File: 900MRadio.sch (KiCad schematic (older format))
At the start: 59 parts, among them P3 BNC, P4 BNC, U3 CC1120, U4 CC1190, U6 0900PC15J0013, U7 EPCOS_B3588, X2 FA-20H32.0000MF20X-K3

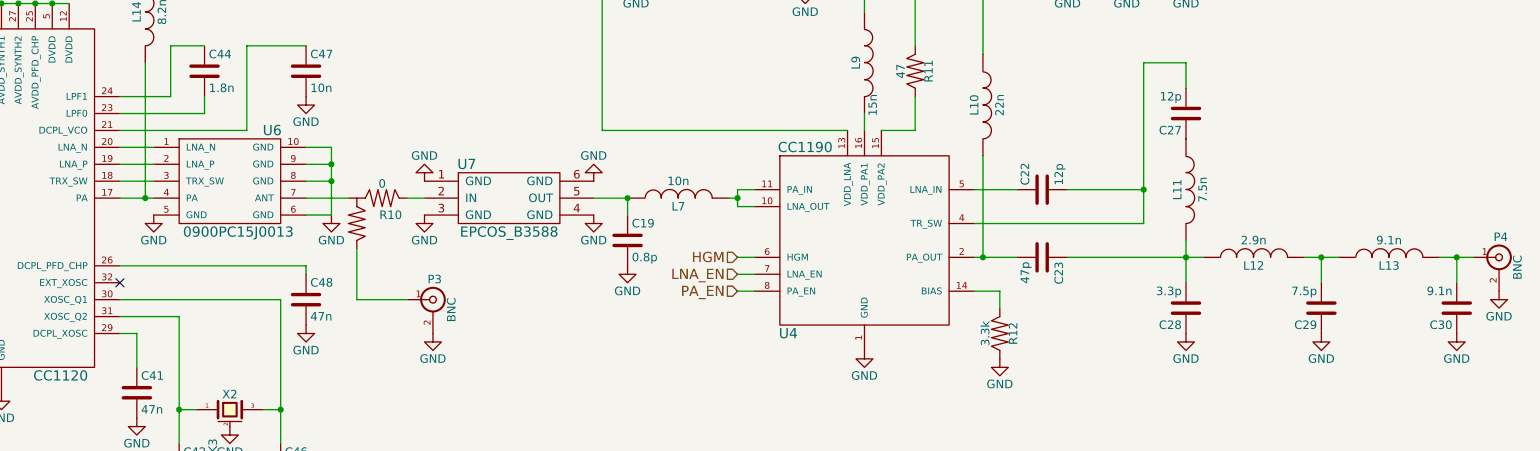
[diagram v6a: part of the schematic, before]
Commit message: Silk cleanup and some more routing finessing.
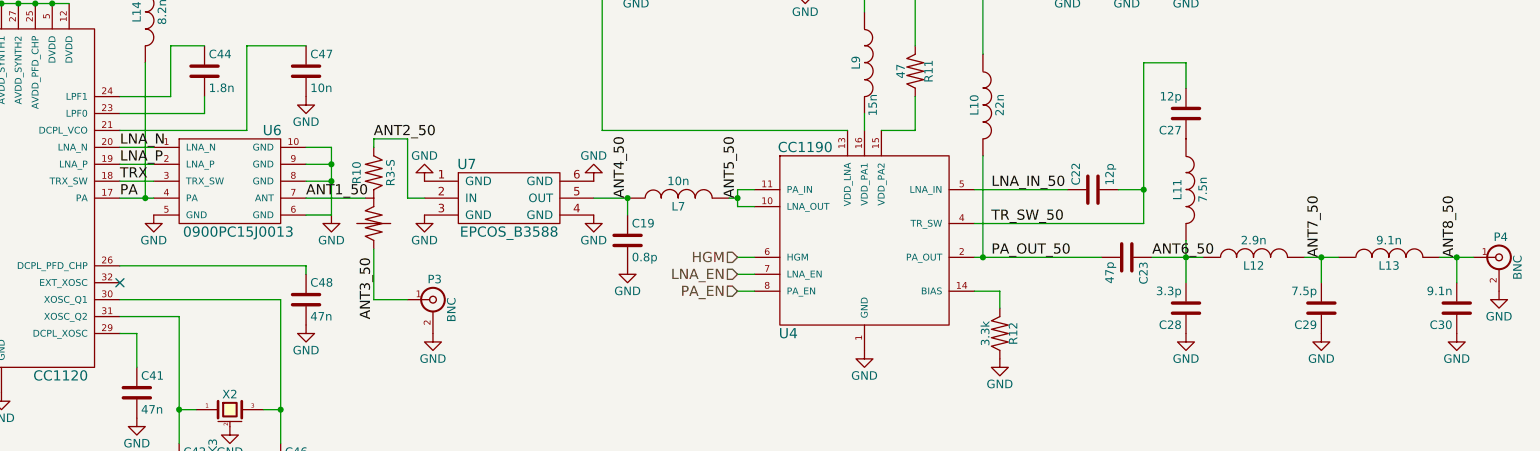
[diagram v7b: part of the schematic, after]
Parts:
- removed R10: 0, Resistors_SMD:R3_LH_0402, symbol R3-LH
- added R10: R3-S, Resistors_SMD:R3_S_0402, symbol R3-S
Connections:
- net PA: now reaches L14.2, U3.17 (PA), U6.4 (PA)
- net TRX: now reaches U3.18 (TRX_SW), U6.3 (TRX_SW)
- net LNA_P: now reaches U3.19 (LNA_P), U6.2 (LNA_P)
- net LNA_N: now reaches U3.20 (LNA_N), U6.1 (LNA_N)
- net ANT5_50: now reaches L7.2, U4.10 (LNA_OUT), U4.11 (PA_IN)
- net PA_OUT_50: now reaches C23.2, L10.2, U4.2 (PA_OUT)
- net TR_SW_50: now reaches C22.2, C27.2, U4.4 (TR_SW)
- net LNA_IN_50: now reaches C22.1, U4.5 (LNA_IN)
- net ANT1_50: now reaches U6.7 (ANT)
- net ANT1_50: now also R10.2
- net ANT8_50: now reaches C30.2, L13.2, P4.1 (In)
- net ANT3_50: now reaches P3.1 (In)
- net ANT3_50: now also R10.3
- net ANT2_50: now reaches U7.2 (IN)
- net ANT2_50: now also R10.1
- net ANT4_50: now reaches C19.1, L7.1, U7.5 (OUT)
- net ANT6_50: now reaches C23.1, C28.2, L11.2, L12.1
- net ANT7_50: now reaches C29.2, L12.2, L13.1
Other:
- moved on the sheet: C22, C23
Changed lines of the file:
@@
-$EndComp
-$Comp
-L R3-LH R10
-U 1 1 55A1928A
-P 4350 3850
-F 0 "R10" H 4300 3950 50  0000 C CNN
-F 1 "0" H 4350 3765 50  0000 C CNN
-F 2 "Resistors_SMD:R3_LH_0402" H 4350 3780 30  0001 C CNN
-F 3 "" V 4350 3850 30  0000 C CNN
-	1    4350 3850
-	-1   0    0    1
 $EndComp
 $Comp
 L C C23
 U 1 1 55A19D87
-P 8250 4200
-F 0 "C23" H 8275 4300 50  0000 L CNN
-F 1 "47p" H 8275 4100 50  0000 L CNN
-F 2 "Capacitors_SMD:C_0402" H 8288 4050 30  0001 C CNN
-F 3 "" H 8250 4200 60  0000 C CNN
-	1    8250 4200
+P 8750 4200
+F 0 "C23" H 8775 4300 50  0000 L CNN
+F 1 "47p" H 8775 4100 50  0000 L CNN
+F 2 "Capacitors_SMD:C_0402" H 8788 4050 30  0001 C CNN
+F 3 "" H 8750 4200 60  0000 C CNN
+	1    8750 4200
 	0    1    1    0
 $EndComp
@@
 L C C22
 U 1 1 55A1A99C
-P 8250 3800
-F 0 "C22" H 8275 3900 50  0000 L CNN
-F 1 "12p" H 8275 3700 50  0000 L CNN
-F 2 "Capacitors_SMD:C_0402" H 8288 3650 30  0001 C CNN
-F 3 "" H 8250 3800 60  0000 C CNN
-	1    8250 3800
+P 8550 3800
+F 0 "C22" H 8575 3900 50  0000 L CNN
+F 1 "12p" H 8575 3700 50  0000 L CNN
+F 2 "Capacitors_SMD:C_0402" H 8588 3650 30  0001 C CNN
+F 3 "" H 8550 3800 60  0000 C CNN
+	1    8550 3800
 	0    -1   -1   0
 $EndComp
@@
 	8000 4400 7850 4400
 Wire Wire Line
-	3900 3850 4150 3850
+	3900 3850 4250 3850
 Wire Wire Line
 	4500 3850 4600 3850
 Wire Wire Line
-	4200 4150 4200 4450
-Wire Wire Line
-	4200 4450 4500 4450
-Wire Wire Line
-	7850 4200 8100 4200
+	4300 4150 4300 4450
+Wire Wire Line
+	4300 4450 4500 4450
+Wire Wire Line
+	7850 4200 8600 4200
 Wire Wire Line
 	7900 4200 7900 3600
 Connection ~ 7900 4200
 Wire Wire Line
-	8400 4200 9200 4200
+	8900 4200 9200 4200
 Wire Wire Line
 	9800 4200 10000 4200
@@
 	9100 3050 9100 3200
 Wire Wire Line
-	7850 3800 8100 3800
-Wire Wire Line
-	8400 3800 8850 3800
+	7850 3800 8400 3800
+Wire Wire Line
+	8700 3800 8850 3800
 Connection ~ 8850 3800
 Wire Wire Line
@@
 Text Label 2650 650  0    60   ~ 0
 VDD_CC1120_ISO
+$Comp
+L R3-S R10
+U 1 1 55A45326
+P 4300 3850
+F 0 "R10" V 4200 3700 50  0000 C CNN
+F 1 "R3-S" V 4400 3700 50  0000 C CNN
+F 2 "Resistors_SMD:R3_S_0402" V 4370 3700 30  0001 C CNN
+F 3 "" H 4300 3700 30  0000 C CNN
+	1    4300 3850
+	1    0    0    1
+$EndComp
+Wire Wire Line
+	4500 3850 4500 3500
+Wire Wire Line
+	4500 3500 4300 3500
+Wire Wire Line
+	4300 3500 4300 3550
+Text Label 2800 3650 0    60   ~ 0
+LNA_P
+Text Label 2800 3550 0    60   ~ 0
+LNA_N
+Text Label 3900 3850 0    60   ~ 0
+ANT1_50
+Text Label 4300 3500 0    60   ~ 0
+ANT2_50
+Text Label 4300 4200 3    60   ~ 0
+ANT3_50
+Text Label 5800 3850 1    60   ~ 0
+ANT4_50
+Text Label 6450 3850 1    60   ~ 0
+ANT5_50
+Text Label 7950 3800 0    60   ~ 0
+LNA_IN_50
+Text Label 7950 4000 0    60   ~ 0
+TR_SW_50
+Text Label 7950 4200 0    60   ~ 0
+PA_OUT_50
+Text Label 8900 4200 0    60   ~ 0
+ANT6_50
+Text Label 9900 4200 1    60   ~ 0
+ANT7_50
+Text Label 10700 4200 1    60   ~ 0
+ANT8_50
+Text Label 2800 3850 0    60   ~ 0
+PA
+Text Label 2800 3750 0    60   ~ 0
+TRX
 $EndSCHEMATC

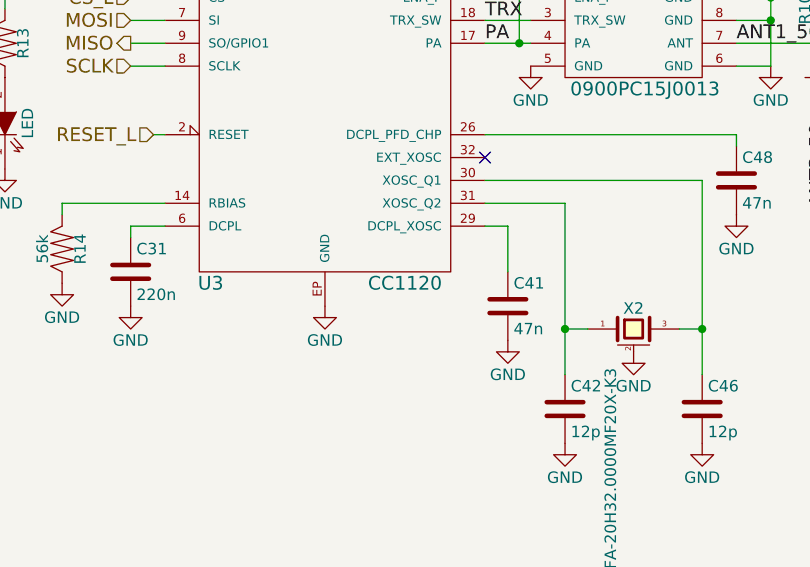
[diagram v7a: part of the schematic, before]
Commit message: Added XMC4500.sch
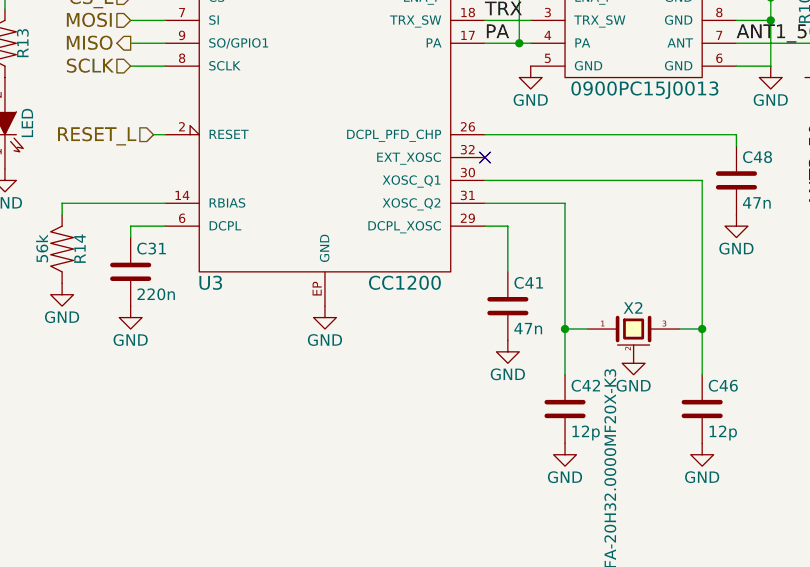
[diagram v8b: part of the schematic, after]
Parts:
- removed U3: CC1120, SMD_Packages:RHB_S-PVQFN-N32, symbol CC1120
- added U3: CC1200, SMD_Packages:RHB_S-PVQFN-N32, symbol CC1200
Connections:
- net CS_L: now also U3.11 (CS)
- net GND: now also U3.EP (GND)
- net GPIO0: now also U3.10 (GPIO0)
- net GPIO2: now also U3.4 (GPIO2)
- net GPIO3: now also U3.3 (GPIO3)
- net LNA_N: now also U3.20 (LNA_N)
- net LNA_P: now also U3.19 (LNA_P)
- net MISO: now also U3.9 (SO/GPIO1)
- net MOSI: now also U3.7 (SI)
- net PA: now also U3.17 (PA)
- net RESET_L: now also U3.2 (RESET)
- net SCLK: now also U3.8 (SCLK)
- net TRX: now also U3.18 (TRX_SW)
- net VDD_CC1120_ISO: now also U3.1 (VDD_GUARD), U3.12 (DVDD), U3.13 (AVDD_IF), U3.15 (AVDD_RF), U3.22 (AVDD_SYNTH1), U3.25 (AVDD_PFD_CHP), U3.27 (AVDD_SYNTH2), U3.28 (AVDD_XOSC), U3.5 (DVDD)
- net at R14.1: now also U3.14 (RBIAS)
- net at C47.1: now also U3.21 (DCPL_VCO)
- net at C44.2: now also U3.23 (LPF0)
- net at C44.1: now also U3.24 (LPF1)
- net at C48.1: now also U3.26 (DCPL_PFD_CHP)
- net at C41.1: now also U3.29 (DCPL_XOSC)
- net at C46.1, X2.3: now also U3.30 (XOSC_Q1)
- net at C42.1, X2.1: now also U3.31 (XOSC_Q2)
- net at C31.1: now also U3.6 (DCPL)
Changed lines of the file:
@@
 LIBS:misc
 LIBS:rf
+LIBS:microcontrollers_xmc
 LIBS:RFBridge-cache
 EELAYER 25 0
@@
 $Descr A4 11693 8268
 encoding utf-8
-Sheet 3 3
+Sheet 3 4
 Title ""
 Date ""
@@
 Comment4 ""
 $EndDescr
-$Comp
-L CC1120 U3
-U 1 1 559BFDEE
-P 2100 3850
-F 0 "U3" H 1600 2800 60  0000 C CNN
-F 1 "CC1120" H 2450 2800 60  0000 C CNN
-F 2 "SMD_Packages:RHB_S-PVQFN-N32" H 2100 3850 60  0001 C CNN
-F 3 "" H 2100 3850 60  0000 C CNN
-	1    2100 3850
-	1    0    0    -1
-$EndComp
 $Comp
 L GND #PWR026
@@
 Text Label 2800 3750 0    60   ~ 0
 TRX
+$Comp
+L CC1200 U3
+U 1 1 55B838F7
+P 2100 3850
+F 0 "U3" H 1600 2800 60  0000 C CNN
+F 1 "CC1200" H 2450 2800 60  0000 C CNN
+F 2 "SMD_Packages:RHB_S-PVQFN-N32" H 2100 3850 60  0001 C CNN
+F 3 "" H 2100 3850 60  0000 C CNN
+	1    2100 3850
+	1    0    0    -1
+$EndComp
 $EndSCHEMATC
